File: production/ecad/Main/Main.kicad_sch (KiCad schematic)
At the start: 4 parts, among them J8 61301611821, J9 61301611821

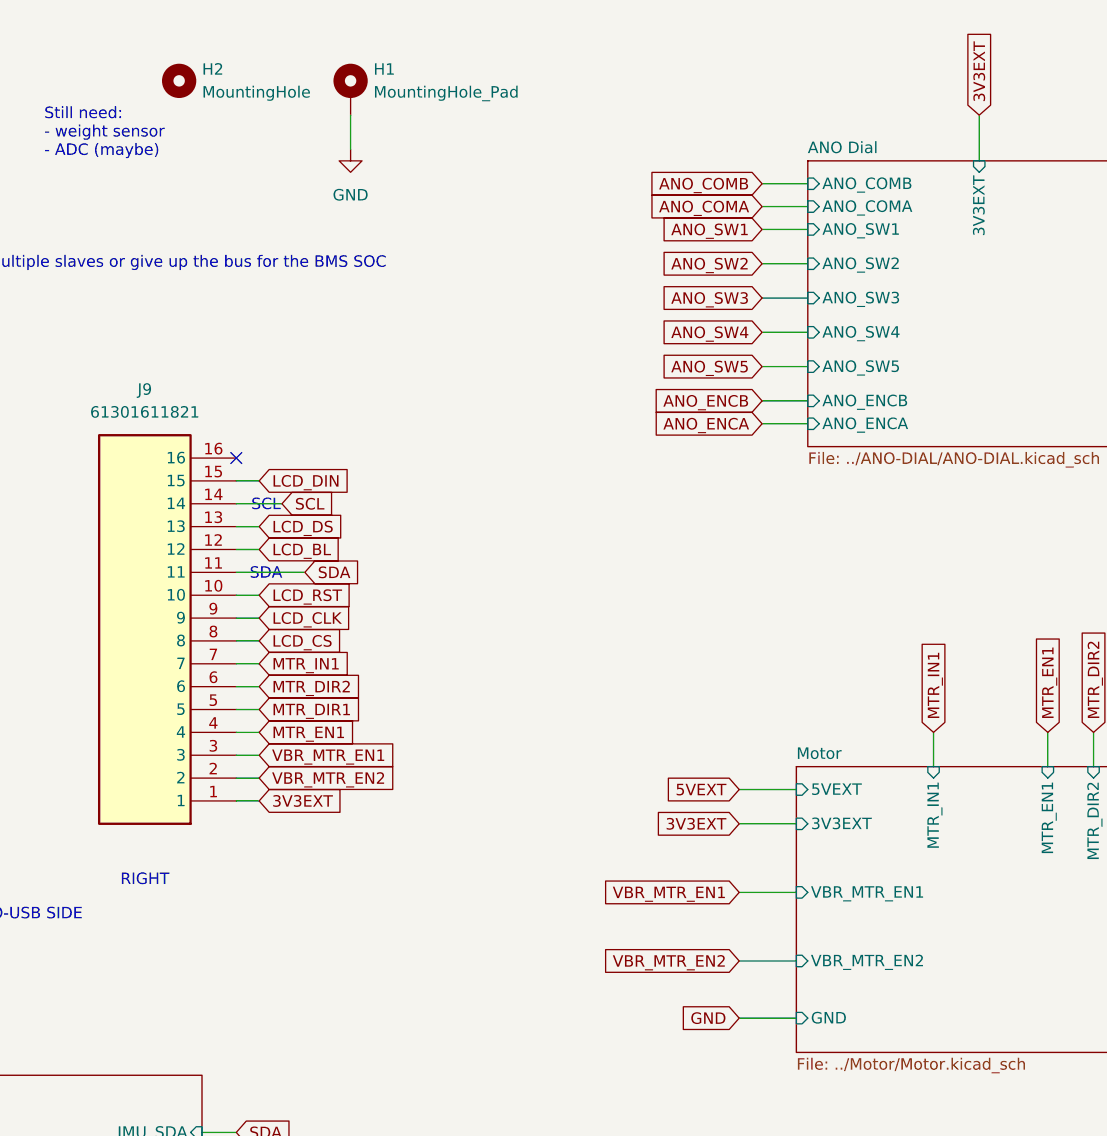
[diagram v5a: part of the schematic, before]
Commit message: i2c pull ups and changes
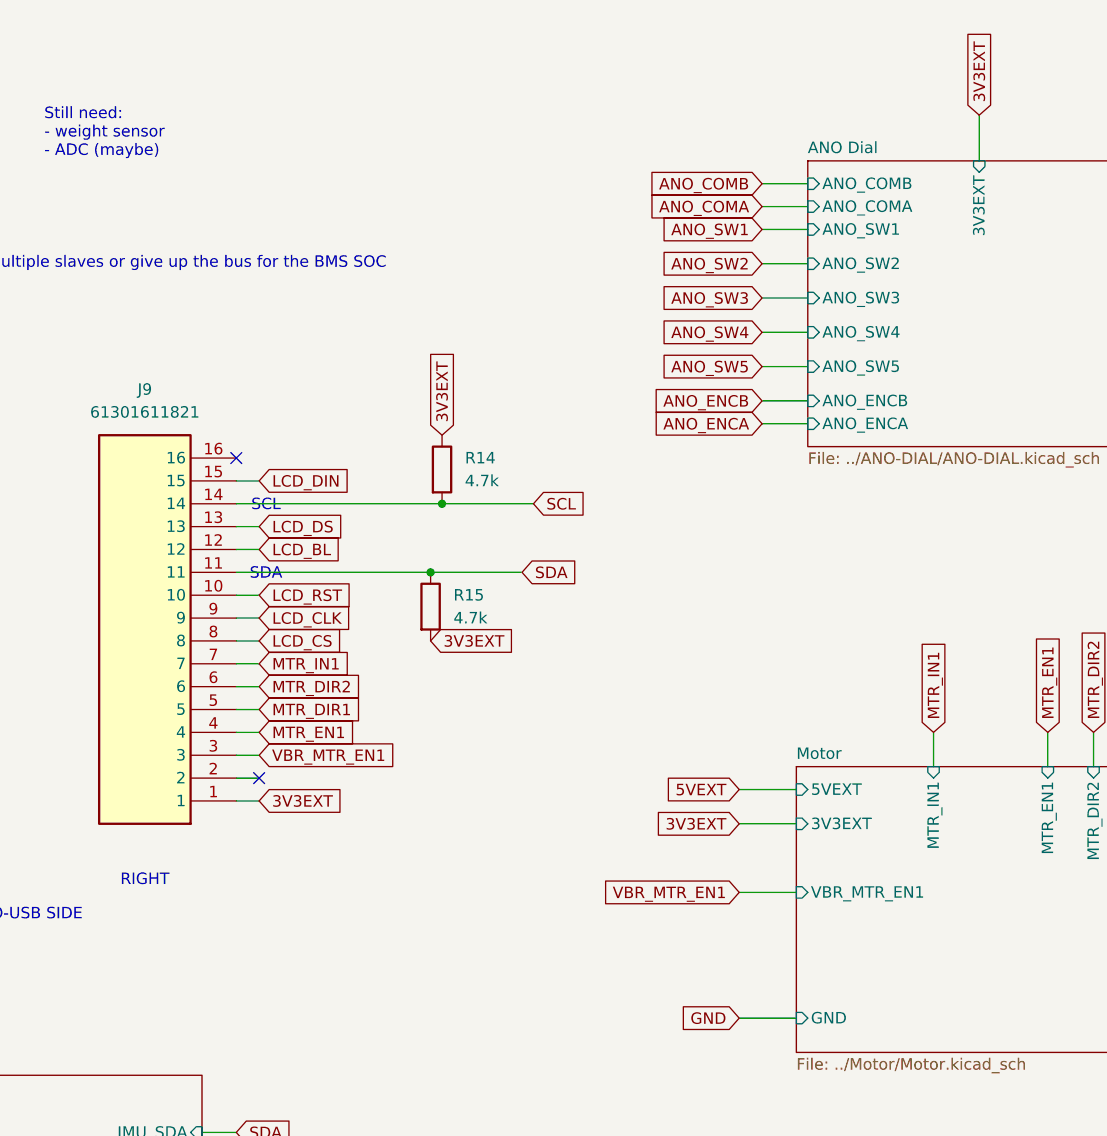
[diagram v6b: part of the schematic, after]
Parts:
- removed H1: MountingHole_Pad, MountingHole:MountingHole_3.5mm_Pad, symbol Mechanical:MountingHole_Pad
- removed H2: MountingHole, MountingHole:MountingHole_3.5mm, symbol Mechanical:MountingHole
- added R14, R15: 4.7k, Resistor_SMD:R_0603_1608Metric_Pad0.98x0.95mm_HandSolder, symbol Device:R
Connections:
- net +3.3V: now also R14.1, R15.2
- net SCL: now also R14.2
- net SDA: now also R15.1
- net VBR_MTR_EN2: no longer names the net of J9.2
- no-connect marks 3 -> 4
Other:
- sheet Motor ports: added none; removed VBR_MTR_EN2
